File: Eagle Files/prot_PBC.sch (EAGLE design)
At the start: 24 parts, among them X1 1501_03, X2 1501_03, X3 1501_03, X4 1501_03, X5 1501_03, X6 1501_03, X7 1501_03, X8 1501_03

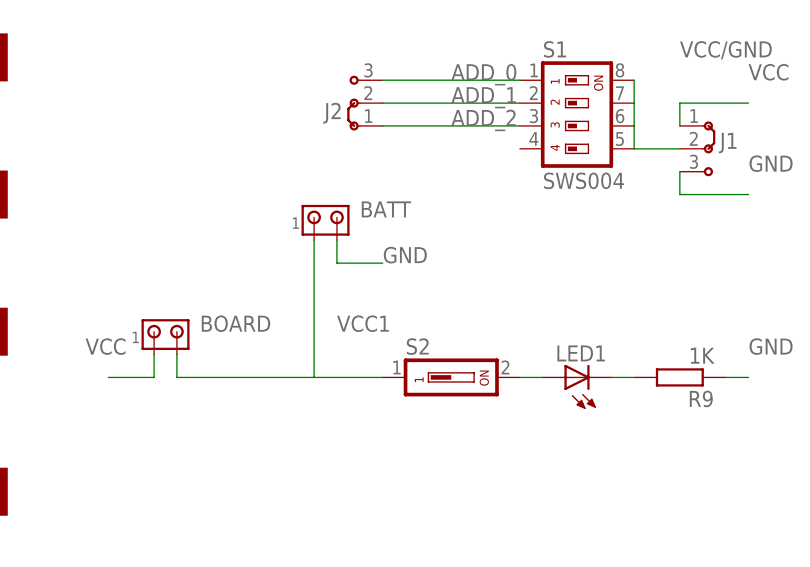
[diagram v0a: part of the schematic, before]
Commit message: 
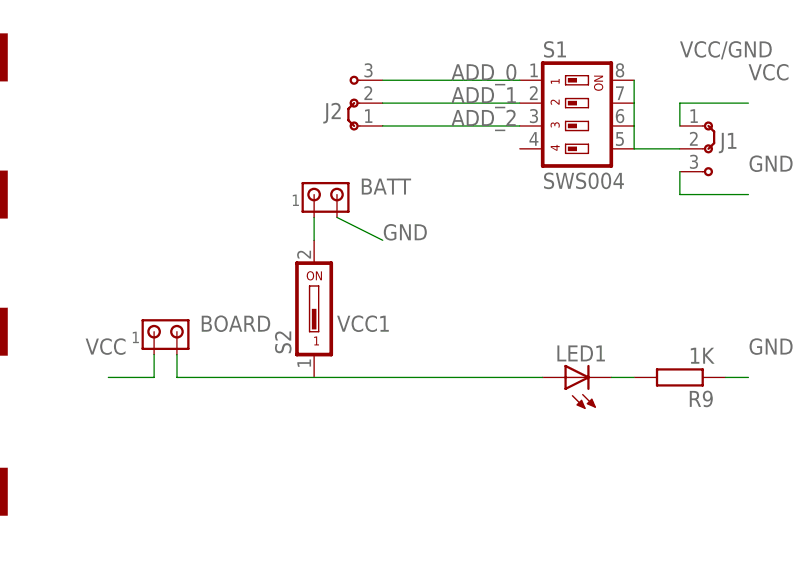
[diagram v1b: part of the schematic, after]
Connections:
- net N$2: now also BATT.1; no longer LED1.A
- net VCC1: now also LED1.A; no longer BATT.1
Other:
- moved on the sheet: BATT, S2
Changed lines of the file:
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@@
 <instance part="LED1" gate="G$1" x="88.9" y="35.56" rot="R90"/>
 <instance part="J1" gate="G$1" x="104.14" y="60.96"/>
-<instance part="S2" gate="G$1" x="76.2" y="35.56" rot="R270"/>
-<instance part="BATT" gate="G$1" x="60.96" y="53.34"/>
+<instance part="S2" gate="G$1" x="60.96" y="43.18"/>
+<instance part="BATT" gate="G$1" x="60.96" y="55.88"/>
 <instance part="BOARD" gate="G$1" x="43.18" y="40.64"/>
 <instance part="J2" gate="G$1" x="66.04" y="66.04" rot="R180"/>
@@
 <segment>
 <pinref part="BATT" gate="G$1" pin="2"/>
-<wire x1="63.5" y1="50.8" x2="63.5" y2="48.26" width="0.1524" layer="91"/>
-<wire x1="63.5" y1="48.26" x2="68.58" y2="48.26" width="0.1524" layer="91"/>
-<label x="68.58" y="48.26" size="1.778" layer="95"/>
+<wire x1="63.5" y1="53.34" x2="68.58" y2="50.8" width="0.1524" layer="91"/>
+<label x="68.58" y="50.8" size="1.778" layer="95"/>
 </segment>
 </net>
@@
 </segment>
 </net>
-<net name="N$2" class="0">
-<segment>
-<pinref part="S2" gate="G$1" pin="2"/>
-<pinref part="LED1" gate="G$1" pin="A"/>
-<wire x1="83.82" y1="35.56" x2="86.36" y2="35.56" width="0.1524" layer="91"/>
-</segment>
-</net>
 <net name="VCC1" class="0">
 <segment>
-<pinref part="S2" gate="G$1" pin="1"/>
-<pinref part="BATT" gate="G$1" pin="1"/>
-<wire x1="60.96" y1="50.8" x2="60.96" y2="35.56" width="0.1524" layer="91"/>
-<wire x1="60.96" y1="35.56" x2="68.58" y2="35.56" width="0.1524" layer="91"/>
 <label x="63.5" y="40.64" size="1.778" layer="95"/>
 <pinref part="BOARD" gate="G$1" pin="2"/>
 <wire x1="45.72" y1="38.1" x2="45.72" y2="35.56" width="0.1524" layer="91"/>
 <wire x1="45.72" y1="35.56" x2="60.96" y2="35.56" width="0.1524" layer="91"/>
-</segment>
-</net>
+<pinref part="S2" gate="G$1" pin="1"/>
+<pinref part="LED1" gate="G$1" pin="A"/>
+<wire x1="86.36" y1="35.56" x2="60.96" y2="35.56" width="0.1524" layer="91"/>
+</segment>
+</net>
+<net name="N$2" class="0">
+<segment>
+<pinref part="BATT" gate="G$1" pin="1"/>
+<pinref part="S2" gate="G$1" pin="2"/>
+<wire x1="60.96" y1="53.34" x2="60.96" y2="50.8" width="0.1524" layer="91"/>
+</segment>
+</net>
